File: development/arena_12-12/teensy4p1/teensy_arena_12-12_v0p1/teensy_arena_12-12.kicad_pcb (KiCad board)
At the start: 4 copper layers, 228.6 x 228.6 mm, 51 parts, among them J1 Barrel_Jack, J2 Conn_01x04, J3 Conn_01x04, P1 CONN15, P10 CONN15, P11 CONN15, P12 CONN15, P2 CONN15, P3 CONN15, P4 CONN15, P5 CONN15, P6 CONN15, P7 CONN15, P8 CONN15, P9 CONN15, Q2 MOSFET_NCHAN, SW1 SW_SPDT, U1 TXB0108PW, U18 Teensy4.1, U2 TXB0108PW, U3 TXB0108PW, U4 TXB0108PW, U5 TXB0108PW

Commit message: Worked on layout for 12-12 NI arena w/ vreg.
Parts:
- moved U18 3.35 mm to (260.3, 270.5)
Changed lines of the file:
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@@
   )
   (footprint "teensy:Teensy41" (layer "F.Cu")
-    (at 259.836926 267.226674 -160)
+    (at 260.310378 270.545439 -160)
     (property "Sheetfile" "teensy.kicad_sch")
     (property "Sheetname" "Teensy")

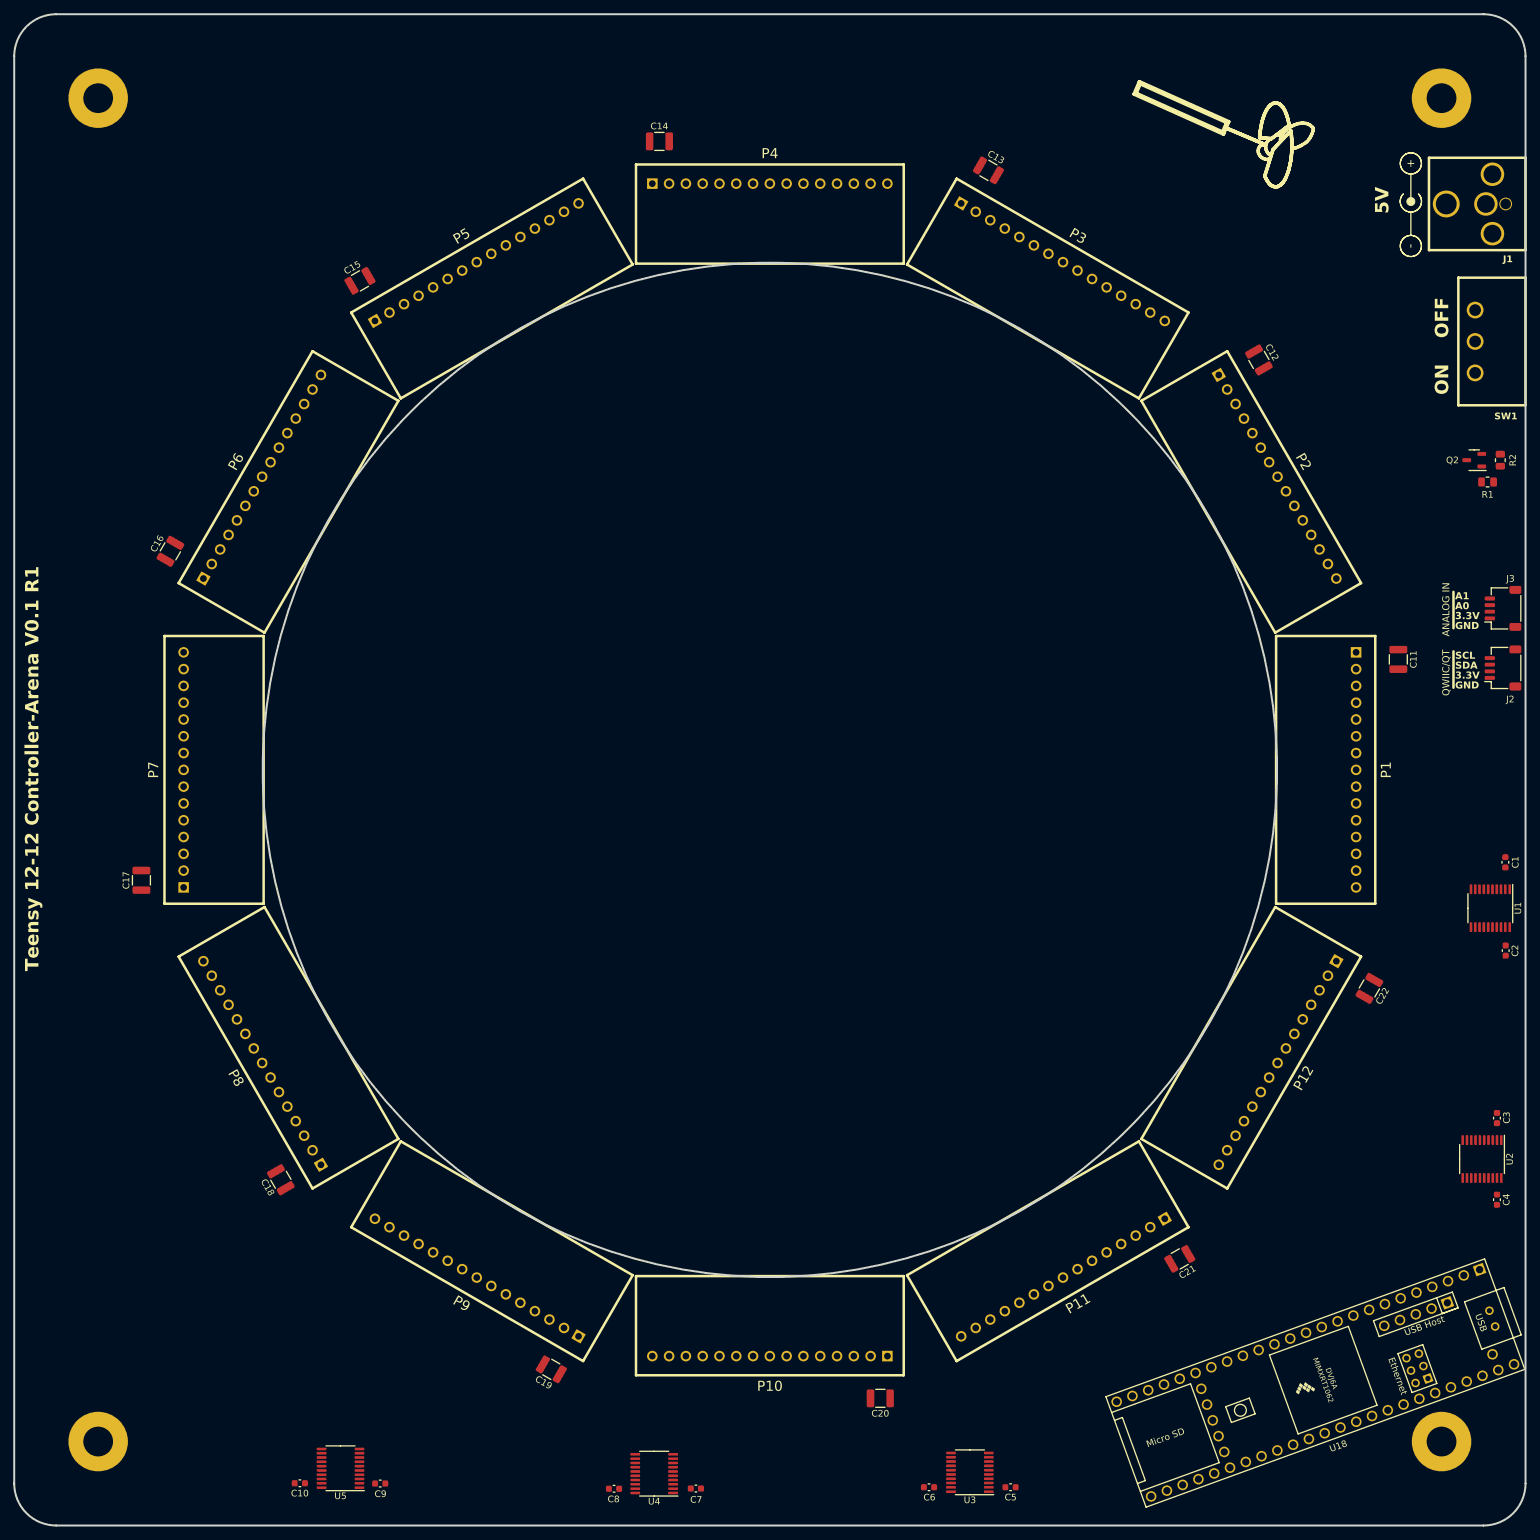
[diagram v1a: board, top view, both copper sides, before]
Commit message: Worked on routing of ni 12-12 arena with vreg.
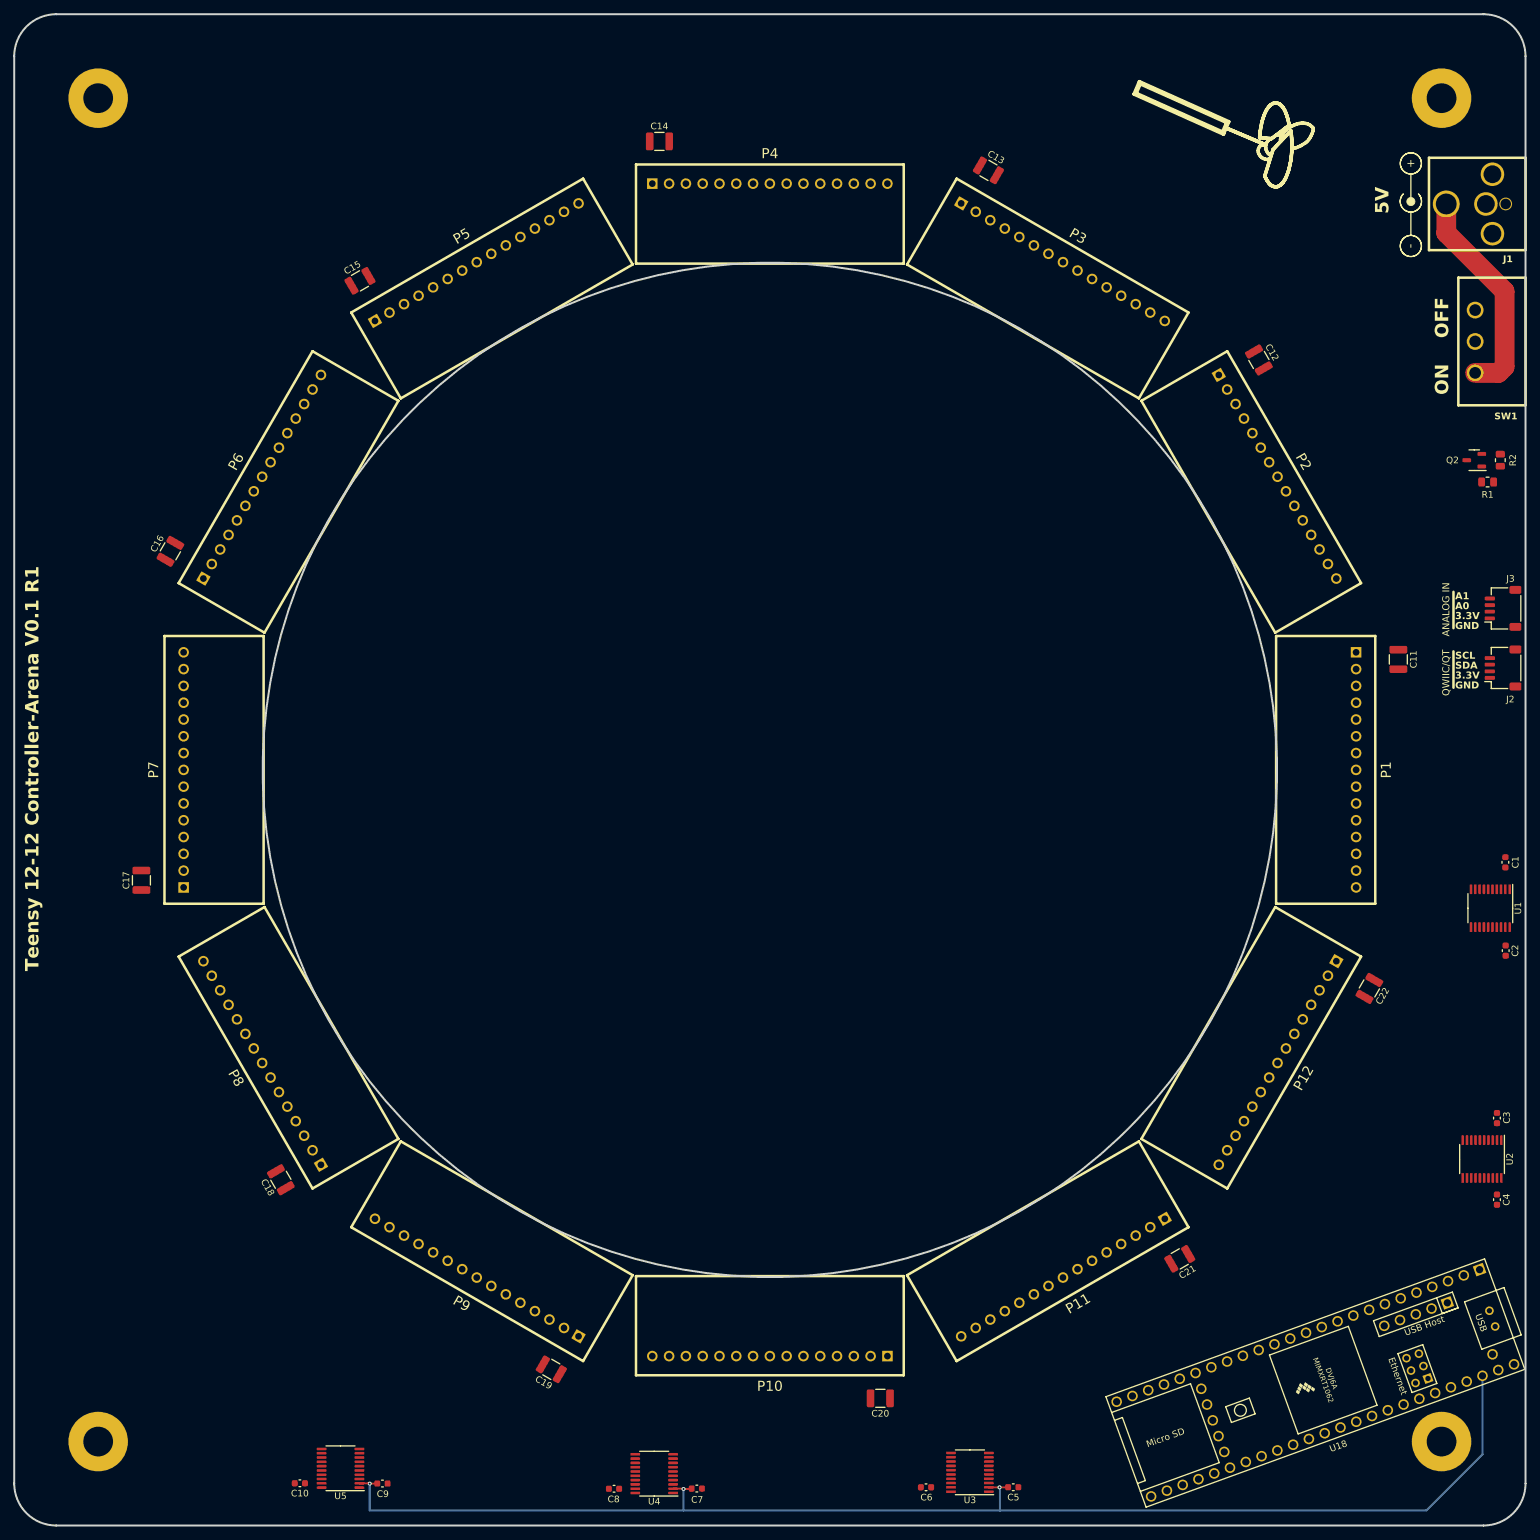
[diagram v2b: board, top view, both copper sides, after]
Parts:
- moved C6 0.45 mm to (201.4, 286.3)
- moved C5 0.41 mm to (214.6, 286.3)
- moved C9 0.34 mm to (119.2, 285.8)
- moved C7 0.14 mm to (166.8, 286.5)
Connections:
- net Net-(SW1-A) renamed /Power/SW_5V
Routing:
- net +3.3V: track 0.00 -> 203.0 mm, vias 0 -> 3
- net /Power/SW_5V: track 0.00 -> 33.1 mm
- added copper zone on In2.Cu, net +5V
- added copper zone on In1.Cu, net GND

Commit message: Added routing of teensy 12-12 arena with big caps.
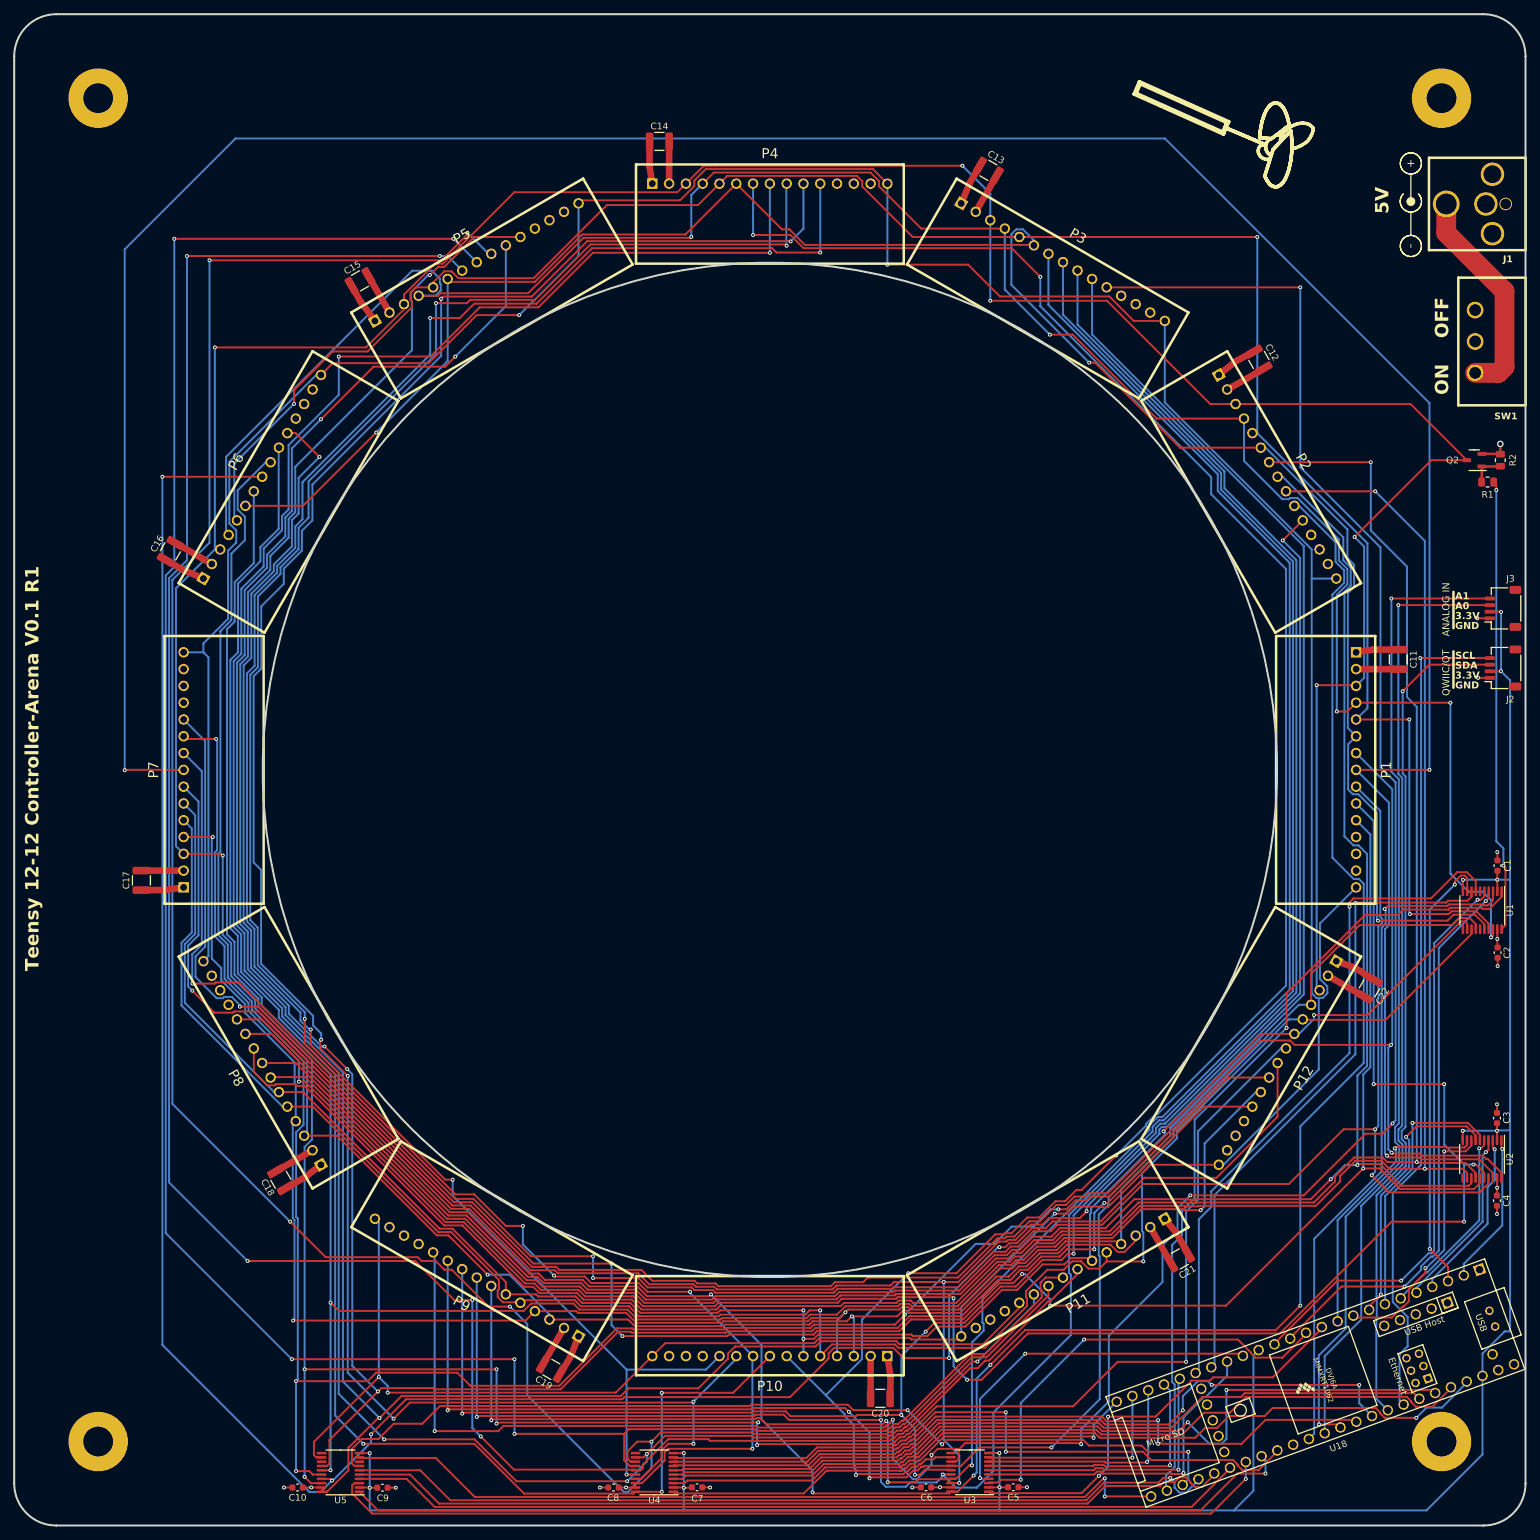
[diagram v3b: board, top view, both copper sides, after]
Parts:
- moved C1 1.29 mm to (287.9, 192.3)
- moved U1 1.26 mm to (285.6, 199.0)
- moved C2 1.26 mm to (287.9, 205.4)
- moved C10 0.73 mm to (106.4, 286.4)
- moved C9 0.63 mm to (119.2, 286.4)
- moved U5 0.63 mm to (112.9, 284.1)
- moved C8 0.21 mm to (154.1, 286.4)
- moved C7 0.19 mm to (166.8, 286.3)
- moved U4 0.19 mm to (160.3, 284.1)
- moved C4 0.15 mm to (287.8, 243.0)
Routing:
- net /Level Shifters/PAN5V.EXT_INT: track 0.00 -> 618.7 mm, vias 0 -> 5
- net /Panel Headers/RESET: track 0.00 -> 613.6 mm, vias 0 -> 8
- net /Level Shifters/PAN5V.CS_01: track 0.00 -> 453.8 mm, vias 0 -> 3
- net /Level Shifters/PAN5V.CS_14: track 0.00 -> 380.7 mm, vias 0 -> 7
- net /Level Shifters/PAN5V.CS_21: track 0.00 -> 370.7 mm, vias 0 -> 5
- net /Level Shifters/PAN5V.CS_26: track 0.00 -> 365.6 mm, vias 0 -> 5
- net /Level Shifters/PAN5V.CS_25: track 0.00 -> 364.2 mm, vias 0 -> 7
- net /Level Shifters/PAN5V.CS_20: track 0.00 -> 364.1 mm, vias 0 -> 5
- net /Level Shifters/PAN5V.CS_22: track 0.00 -> 361.9 mm, vias 0 -> 5
- net /Level Shifters/PAN5V.CS_03: track 0.00 -> 354.9 mm, vias 0 -> 8
- net /Level Shifters/PAN5V.CS_08: track 0.00 -> 348.9 mm, vias 0 -> 5
- net /Level Shifters/PAN5V.CS_16: track 0.00 -> 343.3 mm, vias 0 -> 5
- net /Level Shifters/PAN5V.CS_27: track 0.00 -> 335.3 mm, vias 0 -> 4
- net /Level Shifters/PAN5V.CS_04: track 0.00 -> 334.9 mm, vias 0 -> 6
- net /Level Shifters/PAN5V.CS_07: track 0.00 -> 332.9 mm, vias 0 -> 2
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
